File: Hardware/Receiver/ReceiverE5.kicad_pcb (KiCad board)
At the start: 2 copper layers, 37 parts, among them J1 KBUS, J2 AVR-PDI-6A, J3 CONN_01X08, J4 CONN_01X06, J5 CONN_01X06, J6 CONN_01X04, J7 CONN_01X04, U1 ATXMEGA32E5-A, U2 LM2731, U3 SN74LV07A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

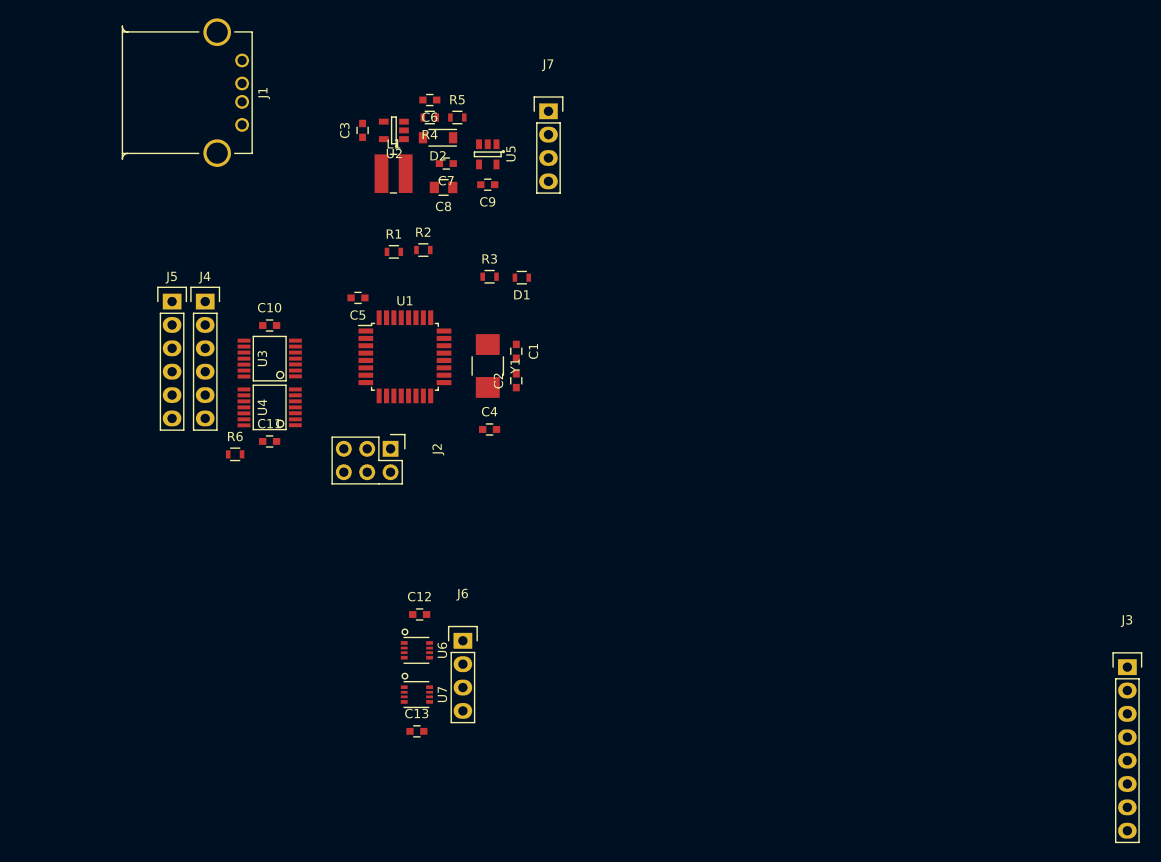
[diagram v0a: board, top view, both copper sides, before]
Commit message: Set up design limits
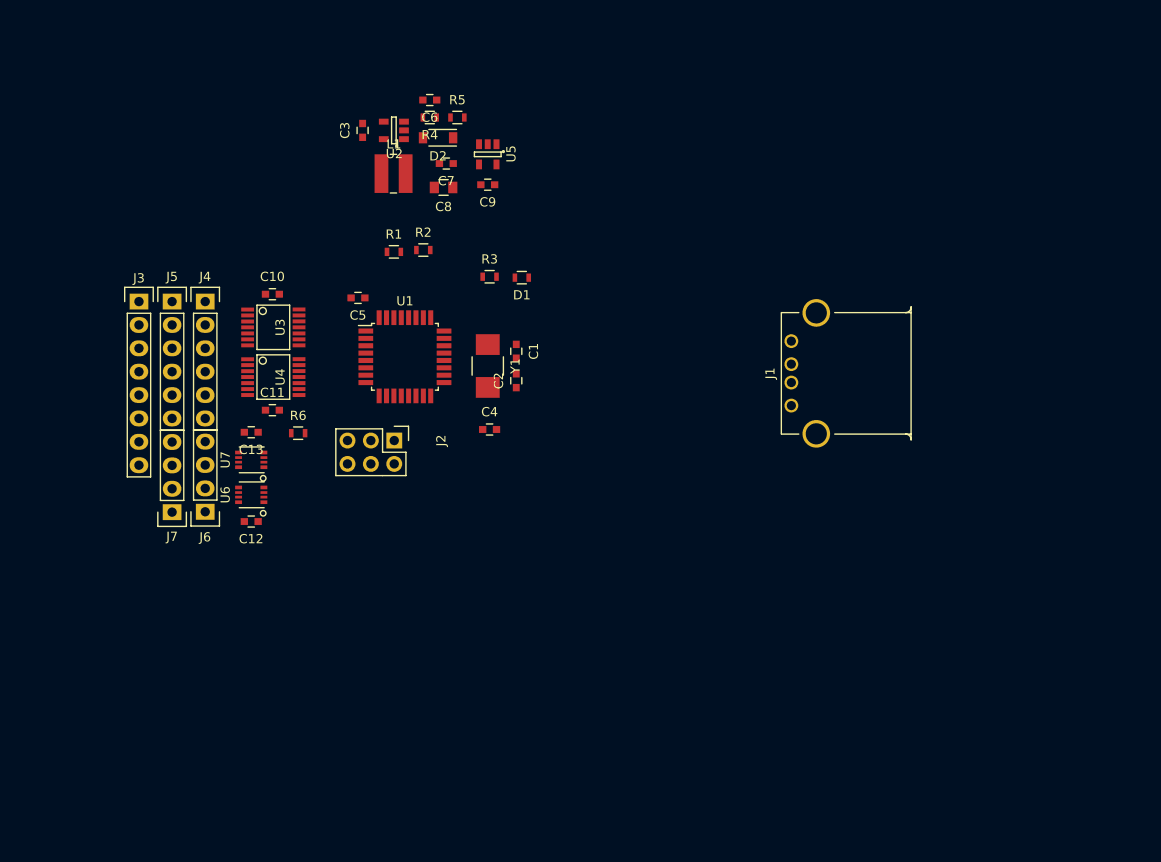
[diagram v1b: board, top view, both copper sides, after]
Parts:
- moved J3 114.5 mm to (72.1, 66.0)
- moved J1 71.9 mm to (145.7, 73.8), turned to 90 degrees
- moved J7 59.8 mm to (75.7, 88.9), turned to 180 degrees
- moved C13 37.2 mm to (84.3, 80.2), turned to 180 degrees
- moved J6 31.3 mm to (79.3, 88.8), turned to 180 degrees
- moved U7 31.2 mm to (84.3, 83.2), turned to 90 degrees
- moved U6 24.7 mm to (84.3, 87.0), turned to 90 degrees
- moved C12 20.9 mm to (84.3, 89.9), turned to 180 degrees
- moved R6 7.23 mm to (89.4, 80.3)
- moved U3 3.42 mm to (86.7, 68.8), turned to 270 degrees
- moved C11 3.41 mm to (86.6, 77.8)
- moved C10 3.41 mm to (86.6, 65.2)
- moved U4 3.32 mm to (86.7, 74.2), turned to 270 degrees
- moved J2 0.98 mm to (99.8, 81.1)
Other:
- net class Default: clearance 0.2 -> 0.1016; trace_width 0.25 -> 0.1016; via_dia 0.6 -> 0.3016; via_drill 0.4 -> 0.2
- rule trace_clearance: 0.2 -> 0.1016
- rule trace_min: 0.2 -> 0.1016
- rule via_min_drill: 0.3 -> 0.2
- rule via_min_size: 0.4 -> 0.2

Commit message: Routing try 1
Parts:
- moved C11 1.53 mm to (86.9, 79.3)
- moved U3 1.30 mm to (85.4, 68.9)
- moved U4 1.30 mm to (85.4, 74.2)
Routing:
- net /C1: track 0.00 -> 21.5 mm, vias 0 -> 2
- net Net-(J5-Pad6): track 0.00 -> 20.1 mm, vias 0 -> 1
- net /C0: track 0.00 -> 18.1 mm, vias 0 -> 2
- net Net-(J5-Pad5): track 0.00 -> 17.5 mm
- net Net-(J5-Pad4): track 0.00 -> 15.5 mm
- net Net-(J5-Pad1): track 0.00 -> 12.5 mm
- net Net-(J5-Pad2): track 0.00 -> 10.5 mm
- net Net-(J5-Pad3): track 0.00 -> 9.75 mm
- net Net-(J4-Pad1): track 0.00 -> 3.97 mm
- net Net-(J4-Pad3): track 0.00 -> 3.67 mm
- net Net-(J4-Pad2): track 0.00 -> 3.46 mm
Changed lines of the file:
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@@
     (thickness 1.6)
     (drawings 0)
-    (tracks 0)
+    (tracks 80)
     (zones 0)
     (modules 37)
@@
   )
   (module Capacitors_SMD:C_0603 (layer F.Cu)
-    (at 86.6 77.8)
+    (at 86.9 79.3)
     (descr "Capacitor SMD 0603, reflow soldering, AVX (see smccp.pdf)")
     (tags "capacitor 0603")
@@
   )
   (module SMD_Packages:SSOP-14 (layer F.Cu)
-    (at 86.7 68.8 270)
+    (at 85.4 68.9 270)
     (attr smd)
     (fp_text reference U3 (at 0 -0.762 270) (layer F.SilkS)
@@
   )
   (module SMD_Packages:SSOP-14 (layer F.Cu)
-    (at 86.7 74.2 270)
+    (at 85.4 74.2 270)
     (attr smd)
     (fp_text reference U4 (at 0 -0.762 270) (layer F.SilkS)
@@
       (net 3 "Net-(C2-Pad1)"))
   )
+  (segment (start 77.5 67.2) (end 77.5 73.8) (width 0.15) (layer B.Cu) (net 15))
+  (segment (start 77.5 73.8) (end 78.4 74.7) (width 0.15) (layer B.Cu) (net 15))
+  (segment (start 78.4 74.7) (end 81.1 74.7) (width 0.15) (layer B.Cu) (net 15))
+  (segment (start 81.1 74.7) (end 81.3 74.9) (width 0.15) (layer B.Cu) (net 15))
+  (via (at 77.5 67.2) (size 0.3016) (drill 0.2) (layers F.Cu B.Cu) (net 15))
+  (segment (start 74.466 67.2) (end 77.5 67.2) (width 0.15) (layer F.Cu) (net 15))
+  (segment (start 73.266 66) (end 74.466 67.2) (width 0.15) (layer F.Cu) (net 15))
+  (segment (start 72.1 66) (end 73.266 66) (width 0.15) (layer F.Cu) (net 15))
+  (via (at 81.3 74.9) (size 0.3016) (drill 0.2) (layers F.Cu B.Cu) (net 15))
+  (segment (start 81.3 74.9) (end 82.5664 74.9) (width 0.15) (layer F.Cu) (net 15))
+  (segment (start 82.5664 74.9) (end 82.606 74.8604) (width 0.15) (layer F.Cu) (net 15))
+  (segment (start 86.8 75.5) (end 88.1859 75.5) (width 0.15) (layer F.Cu) (net 16))
+  (segment (start 88.1859 75.5) (end 88.194 75.5081) (width 0.15) (layer F.Cu) (net 16))
+  (segment (start 80.75161 74.95161) (end 81.3 75.5) (width 0.15) (layer B.Cu) (net 16))
+  (segment (start 81.3 75.5) (end 86.8 75.5) (width 0.15) (layer B.Cu) (net 16))
+  (via (at 86.8 75.5) (size 0.3016) (drill 0.2) (layers F.Cu B.Cu) (net 16))
+  (segment (start 78.29578 74.95161) (end 80.75161 74.95161) (width 0.15) (layer B.Cu) (net 16))
+  (segment (start 77.3 74.3) (end 77.95161 74.95161) (width 0.15) (layer B.Cu) (net 16))
+  (segment (start 77.95161 74.95161) (end 78.29578 74.95161) (width 0.15) (layer B.Cu) (net 16))
+  (segment (start 77.24839 74.3) (end 77.3 74.3) (width 0.15) (layer B.Cu) (net 16))
+  (segment (start 77.24839 70.04839) (end 77.24839 74.3) (width 0.15) (layer B.Cu) (net 16))
+  (segment (start 77 69.8) (end 77.24839 70.04839) (width 0.15) (layer B.Cu) (net 16))
+  (segment (start 72.1 68.54) (end 73.266 68.54) (width 0.15) (layer F.Cu) (net 16))
+  (segment (start 73.266 68.54) (end 74.526 69.8) (width 0.15) (layer F.Cu) (net 16))
+  (segment (start 74.526 69.8) (end 77 69.8) (width 0.15) (layer F.Cu) (net 16))
+  (via (at 77 69.8) (size 0.3016) (drill 0.2) (layers F.Cu B.Cu) (net 16))
+  (segment (start 80.4 66.2471) (end 79.5471 66.2471) (width 0.15) (layer F.Cu) (net 23))
+  (segment (start 79.5471 66.2471) (end 79.3 66) (width 0.15) (layer F.Cu) (net 23))
+  (segment (start 82.606 67.6046) (end 81.7575 67.6046) (width 0.15) (layer F.Cu) (net 23))
+  (segment (start 81.7575 67.6046) (end 80.4 66.2471) (width 0.15) (layer F.Cu) (net 23))
+  (segment (start 82.606 68.9) (end 79.66 68.9) (width 0.15) (layer F.Cu) (net 24))
+  (segment (start 79.66 68.9) (end 79.3 68.54) (width 0.15) (layer F.Cu) (net 24))
+  (segment (start 82.606 70.2081) (end 80.1719 70.2081) (width 0.15) (layer F.Cu) (net 25))
+  (segment (start 80.1719 70.2081) (end 79.3 71.08) (width 0.15) (layer F.Cu) (net 25))
+  (segment (start 82.606 72.9046) (end 81.7575 72.9046) (width 0.15) (layer F.Cu) (net 29))
+  (segment (start 81.7575 72.9046) (end 80.97311 72.12021) (width 0.15) (layer F.Cu) (net 29))
+  (segment (start 80.97311 72.12021) (end 78.716731 72.12021) (width 0.15) (layer F.Cu) (net 29))
+  (segment (start 78.716731 72.12021) (end 77.9 71.303479) (width 0.15) (layer F.Cu) (net 29))
+  (segment (start 77.9 71.303479) (end 77.9 66.6) (width 0.15) (layer F.Cu) (net 29))
+  (segment (start 77.9 66.6) (end 77.3 66) (width 0.15) (layer F.Cu) (net 29))
+  (segment (start 77.3 66) (end 75.7 66) (width 0.15) (layer F.Cu) (net 29))
+  (segment (start 82.606 74.2) (end 81.7575 74.2) (width 0.15) (layer F.Cu) (net 30))
+  (segment (start 81.7575 74.2) (end 79.92932 72.37182) (width 0.15) (layer F.Cu) (net 30))
+  (segment (start 77.4 71.159309) (end 77.4 69.074) (width 0.15) (layer F.Cu) (net 30))
+  (segment (start 79.92932 72.37182) (end 78.61251 72.371819) (width 0.15) (layer F.Cu) (net 30))
+  (segment (start 78.61251 72.371819) (end 77.4 71.159309) (width 0.15) (layer F.Cu) (net 30))
+  (segment (start 77.4 69.074) (end 76.866 68.54) (width 0.15) (layer F.Cu) (net 30))
+  (segment (start 76.866 68.54) (end 75.7 68.54) (width 0.15) (layer F.Cu) (net 30))
+  (segment (start 82.606 75.5081) (end 80.731159 75.5081) (width 0.15) (layer F.Cu) (net 31))
+  (segment (start 80.731159 75.5081) (end 79.883269 74.66021) (width 0.15) (layer F.Cu) (net 31))
+  (segment (start 79.883269 74.66021) (end 78.716731 74.66021) (width 0.15) (layer F.Cu) (net 31))
+  (segment (start 78.716731 74.66021) (end 77.5 73.443479) (width 0.15) (layer F.Cu) (net 31))
+  (segment (start 77.5 73.443479) (end 77.5 71.714) (width 0.15) (layer F.Cu) (net 31))
+  (segment (start 77.5 71.714) (end 76.866 71.08) (width 0.15) (layer F.Cu) (net 31))
+  (segment (start 76.866 71.08) (end 75.7 71.08) (width 0.15) (layer F.Cu) (net 31))
+  (segment (start 77.7 74.3) (end 77.02 73.62) (width 0.15) (layer F.Cu) (net 32))
+  (segment (start 77.02 73.62) (end 75.7 73.62) (width 0.15) (layer F.Cu) (net 32))
+  (segment (start 77.7 76.183479) (end 77.7 74.3) (width 0.15) (layer F.Cu) (net 32))
+  (segment (start 88.194 76.1558) (end 86.417599 76.1558) (width 0.15) (layer F.Cu) (net 32))
+  (segment (start 86.417599 76.1558) (end 85.373189 77.20021) (width 0.15) (layer F.Cu) (net 32))
+  (segment (start 85.373189 77.20021) (end 78.716731 77.20021) (width 0.15) (layer F.Cu) (net 32))
+  (segment (start 78.716731 77.20021) (end 77.7 76.183479) (width 0.15) (layer F.Cu) (net 32))
+  (segment (start 88.7 77.5) (end 78.206 77.5) (width 0.15) (layer F.Cu) (net 33))
+  (segment (start 78.206 77.5) (end 76.866 76.16) (width 0.15) (layer F.Cu) (net 33))
+  (segment (start 76.866 76.16) (end 75.7 76.16) (width 0.15) (layer F.Cu) (net 33))
+  (segment (start 89.4 76.8) (end 88.7 77.5) (width 0.15) (layer F.Cu) (net 33))
+  (segment (start 89.4 75.2179) (end 89.4 76.8) (width 0.15) (layer F.Cu) (net 33))
+  (segment (start 88.194 74.8604) (end 89.0425 74.8604) (width 0.15) (layer F.Cu) (net 33))
+  (segment (start 89.0425 74.8604) (end 89.4 75.2179) (width 0.15) (layer F.Cu) (net 33))
+  (segment (start 81.3 77.82741) (end 81.3 77.614147) (width 0.15) (layer B.Cu) (net 34))
+  (segment (start 81.3 77.614147) (end 81.185853 77.5) (width 0.15) (layer B.Cu) (net 34))
+  (segment (start 81.185853 77.5) (end 75.8864 77.5) (width 0.15) (layer B.Cu) (net 34))
+  (segment (start 75.8864 77.5) (end 75.7 77.6864) (width 0.15) (layer B.Cu) (net 34))
+  (segment (start 75.7 77.6864) (end 75.7 78.7) (width 0.15) (layer B.Cu) (net 34))
+  (segment (start 88.194 73.5523) (end 89.0425 73.5523) (width 0.15) (layer F.Cu) (net 34))
+  (segment (start 89.0425 73.5523) (end 89.651609 74.161409) (width 0.15) (layer F.Cu) (net 34))
+  (segment (start 89.651609 74.161409) (end 89.651609 76.904221) (width 0.15) (layer F.Cu) (net 34))
+  (segment (start 89.651609 76.904221) (end 88.72842 77.82741) (width 0.15) (layer F.Cu) (net 34))
+  (segment (start 88.72842 77.82741) (end 81.3 77.82741) (width 0.15) (layer F.Cu) (net 34))
+  (via (at 81.3 77.82741) (size 0.3016) (drill 0.2) (layers F.Cu B.Cu) (net 34))
 )

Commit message: Routing try 2
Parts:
- moved U1 4.70 mm to (96.3, 71.8)
- moved C5 3.61 mm to (92.3, 65.3)
- moved C11 1.92 mm to (86.0, 77.6)
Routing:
- net /C4: track 0.00 -> 44.3 mm, vias 0 -> 3
- net /C2: track 0.00 -> 43.3 mm, vias 0 -> 5
- net /C5: track 0.00 -> 40.7 mm, vias 0 -> 4
- net /C3: track 0.00 -> 34.3 mm, vias 0 -> 4
- net /C6: track 0.00 -> 31.3 mm, vias 0 -> 2
- net /C7: track 0.00 -> 30.9 mm, vias 0 -> 2
- net /C0: track 18.1 -> 42.6 mm, vias 2 -> 4
- net /A7: track 0.00 -> 21.7 mm, vias 0 -> 2
- net /A6: track 0.00 -> 19.7 mm, vias 0 -> 2
- net Net-(J4-Pad6): track 0.00 -> 19.3 mm, vias 0 -> 2
- net /C1: track 21.5 -> 37.2 mm, vias 2 -> 4
- net /A0: track 0.00 -> 15.2 mm, vias 0 -> 2
- net Net-(J4-Pad5): track 0.00 -> 14.1 mm, vias 0 -> 3
- net /A1: track 0.00 -> 12.8 mm, vias 0 -> 2
- net Net-(J4-Pad4): track 0.00 -> 11.3 mm, vias 0 -> 1
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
